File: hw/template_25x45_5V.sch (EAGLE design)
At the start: 25 parts, among them J1 GROVE-4P-2.0-3470130P1, J2 GROVE-4P-2.0-3470130P1, U5 LD3985XX

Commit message: Updated to R2P Eagle libraries
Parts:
- C1: value (none) -> 1u; device rcl:C-EUC1206 -> r2p_rcl:C-1206
- C14, C17, C18, C19, C2, C3, C4, C6, C7, C8: device rcl:C-EUC0603 -> r2p_rcl:C-0603
- C5: device rcl:C-EUC0805 -> r2p_rcl:C-0805
- C9: value (none) -> 10u; device rcl:C-EUC0805 -> r2p_rcl:C-0805
- J1, J2: value GROVE-4P-2.0-3470130P1 -> R2P_BUS-VERTICAL; device OPL Eagle Library:GROVE-4P-2.0-3470130P1 -> r2p_connector:R2P_BUS-VERTICAL
- LED1: value (none) -> LED0805; device led:LEDCHIPLED_0805 -> r2p_led:LED0805
- R1: device rcl:R-EU_R0603 -> r2p_rcl:R-0603
- SOT1: device maxim:MAX3051EKA -> r2p_ic:MAX3051EKA
- U$2: device coilcraft:LPS4018 -> r2p_rcl:LPS4018
- U$3: device maxim:MAX17501 -> r2p_ic:MAX17501
- U$4: value FTSH-105TH -> JTAG-TH; device samtec:FTSH-105TH -> r2p_connector:JTAG-TH
- U$5: value ASD -> ABRACON_ASD; device abracon:ASD -> r2p_ic:ABRACON_ASD
- U$6: value STM32F103CXTX -> STM32F303CTX; device st:STM32F103CXTX -> r2p_ic:STM32F303CTX
- U5: value LD3985XX -> TLV700XXDDC; device st:LD3985XX -> r2p_ic:TLV700XXDDC
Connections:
- net VIN renamed +VBUS
- net +3V3: now also U$4.1; no longer U$4.P$1
- net +5V: now also U5.EN; no longer U5.INHIBIT
- net GND: now also U$4.3, U$4.5, U$4.7, U$4.9; no longer U$4.P$3, U$4.P$5, U$4.P$7, U$4.P$9
- net JTCK: now also U$4.4; no longer U$4.P$4
- net JTDI: now also U$4.8; no longer U$4.P$8
- net JTDO: now also U$4.6; no longer U$4.P$6
- net JTMS: now also U$4.2; no longer U$4.P$2
- net LED1: now also U$6.PF1/OSC_OUT; no longer U$6.PD1/OSC_OUT
- net NRST: now also U$4.10; no longer U$4.P$10
- net OSC_IN: now also U$6.PF0/OSC_IN; no longer U$6.PD0/OSC_IN

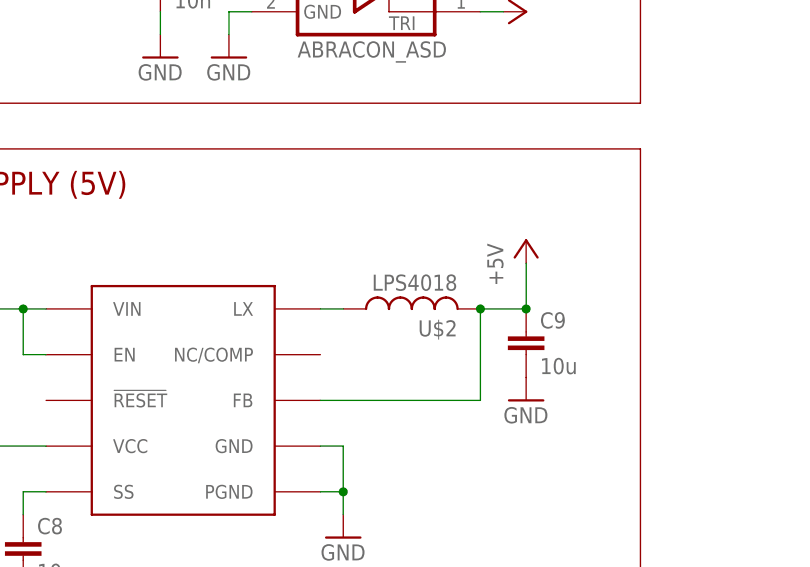
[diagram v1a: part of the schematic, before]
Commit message: Updated keepout
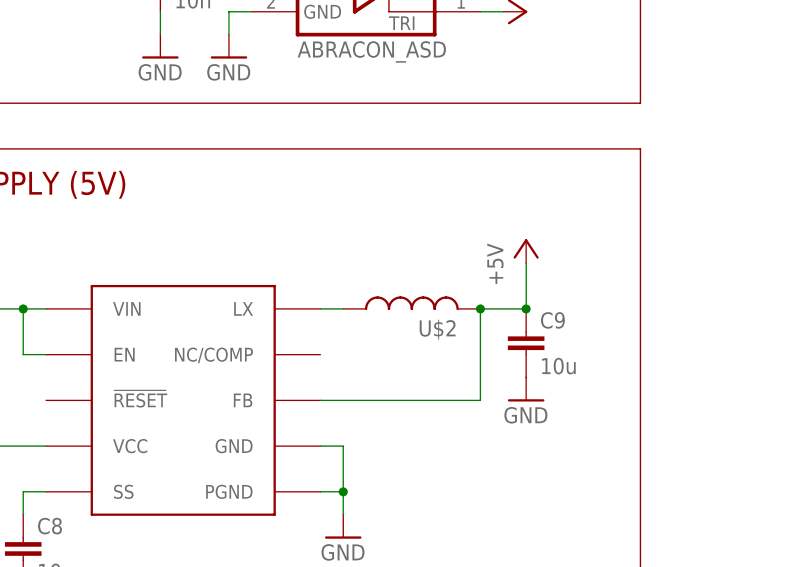
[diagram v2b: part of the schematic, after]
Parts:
- C1: device r2p_rcl:C-1206 -> r2p_rcl:C1206
- C14, C17, C18, C19, C2, C3, C4, C6, C7, C8: device r2p_rcl:C-0603 -> r2p_rcl:C0603
- C5, C9: device r2p_rcl:C-0805 -> r2p_rcl:C0805
- R1: device r2p_rcl:R-0603 -> r2p_rcl:R0603
- U$2: value LPS4018 -> (none)
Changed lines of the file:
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@@
 </classes>
 <parts>
-<part name="C6" library="r2p_rcl" deviceset="C" device="-0603" value="10n"/>
+<part name="C6" library="r2p_rcl" deviceset="C" device="0603" value="10n"/>
 <part name="GND11" library="r2p_supply" deviceset="GND" device=""/>
 <part name="GND12" library="r2p_supply" deviceset="GND" device=""/>
@@
 <part name="GND6" library="r2p_supply" deviceset="GND" device=""/>
 <part name="+3V4" library="r2p_supply" deviceset="+3V3" device=""/>
-<part name="C17" library="r2p_rcl" deviceset="C" device="-0603" value="100n"/>
-<part name="C14" library="r2p_rcl" deviceset="C" device="-0603" value="100n"/>
-<part name="C4" library="r2p_rcl" deviceset="C" device="-0603" value="100n"/>
+<part name="C17" library="r2p_rcl" deviceset="C" device="0603" value="100n"/>
+<part name="C14" library="r2p_rcl" deviceset="C" device="0603" value="100n"/>
+<part name="C4" library="r2p_rcl" deviceset="C" device="0603" value="100n"/>
 <part name="GND29" library="r2p_supply" deviceset="GND" device=""/>
 <part name="GND30" library="r2p_supply" deviceset="GND" device=""/>
 <part name="GND31" library="r2p_supply" deviceset="GND" device=""/>
 <part name="+3V11" library="r2p_supply" deviceset="+3V3" device=""/>
-<part name="C5" library="r2p_rcl" deviceset="C" device="-0805" value="4.7u"/>
+<part name="C5" library="r2p_rcl" deviceset="C" device="0805" value="4.7u"/>
 <part name="GND34" library="r2p_supply" deviceset="GND" device=""/>
 <part name="+3V5" library="r2p_supply" deviceset="+3V3" device=""/>
 <part name="GND7" library="r2p_supply" deviceset="GND" device=""/>
 <part name="+3V6" library="r2p_supply" deviceset="+3V3" device=""/>
-<part name="C3" library="r2p_rcl" deviceset="C" device="-0603" value="100n"/>
+<part name="C3" library="r2p_rcl" deviceset="C" device="0603" value="100n"/>
 <part name="GND9" library="r2p_supply" deviceset="GND" device=""/>
 <part name="+3V3" library="r2p_supply" deviceset="+3V3" device=""/>
 <part name="GND8" library="r2p_supply" deviceset="GND" device=""/>
 <part name="GND10" library="r2p_supply" deviceset="GND" device=""/>
-<part name="C7" library="r2p_rcl" deviceset="C" device="-0603" value="100n"/>
+<part name="C7" library="r2p_rcl" deviceset="C" device="0603" value="100n"/>
 <part name="GND22" library="r2p_supply" deviceset="GND" device=""/>
 <part name="LED1" library="r2p_led" deviceset="LED" device="0805" value=""/>
-<part name="R1" library="r2p_rcl" deviceset="R" device="-0603" value="330"/>
+<part name="R1" library="r2p_rcl" deviceset="R" device="0603" value="330"/>
 <part name="GND16" library="r2p_supply" deviceset="GND" device=""/>
 <part name="GND17" library="r2p_supply" deviceset="GND" device=""/>
@@
 <part name="J2" library="r2p_connector" deviceset="R2P_BUS" device="-VERTICAL"/>
 <part name="U$2" library="r2p_rcl" deviceset="LPS4018" device=""/>
-<part name="C1" library="r2p_rcl" deviceset="C" device="-1206" value="1u"/>
+<part name="C1" library="r2p_rcl" deviceset="C" device="1206" value="1u"/>
 <part name="GND1" library="r2p_supply" deviceset="GND" device=""/>
-<part name="C2" library="r2p_rcl" deviceset="C" device="-0603" value="1u"/>
-<part name="C8" library="r2p_rcl" deviceset="C" device="-0603" value="10n"/>
+<part name="C2" library="r2p_rcl" deviceset="C" device="0603" value="1u"/>
+<part name="C8" library="r2p_rcl" deviceset="C" device="0603" value="10n"/>
 <part name="GND4" library="r2p_supply" deviceset="GND" device=""/>
 <part name="GND5" library="r2p_supply" deviceset="GND" device=""/>
-<part name="C9" library="r2p_rcl" deviceset="C" device="-0805" value="10u"/>
+<part name="C9" library="r2p_rcl" deviceset="C" device="0805" value="10u"/>
 <part name="GND2" library="r2p_supply" deviceset="GND" device=""/>
 <part name="GND3" library="r2p_supply" deviceset="GND" device=""/>
@@
 <part name="GND25" library="r2p_supply" deviceset="GND" device=""/>
 <part name="+3V9" library="r2p_supply" deviceset="+3V3" device=""/>
-<part name="C18" library="r2p_rcl" deviceset="C" device="-0603" value="1u"/>
-<part name="C19" library="r2p_rcl" deviceset="C" device="-0603" value="1u"/>
+<part name="C18" library="r2p_rcl" deviceset="C" device="0603" value="1u"/>
+<part name="C19" library="r2p_rcl" deviceset="C" device="0603" value="1u"/>
 <part name="GND26" library="r2p_supply" deviceset="GND" device=""/>
 <part name="GND28" library="r2p_supply" deviceset="GND" device=""/>
